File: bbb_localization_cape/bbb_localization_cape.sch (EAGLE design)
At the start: 32 parts, among them J2 MOLEX-22-03-5035, U1 SN65HVD256DR, U2 ARDUCAMOV5642, U3 SN74LV1T126DCKR, U4 MSP430G2553IPW20R, U5 SN74LV1T125DCKR, U6 LP38693MP-3.3/NOPB, U7 LM1085ISX-ADJ, U8 SN74LV1T126DCKR

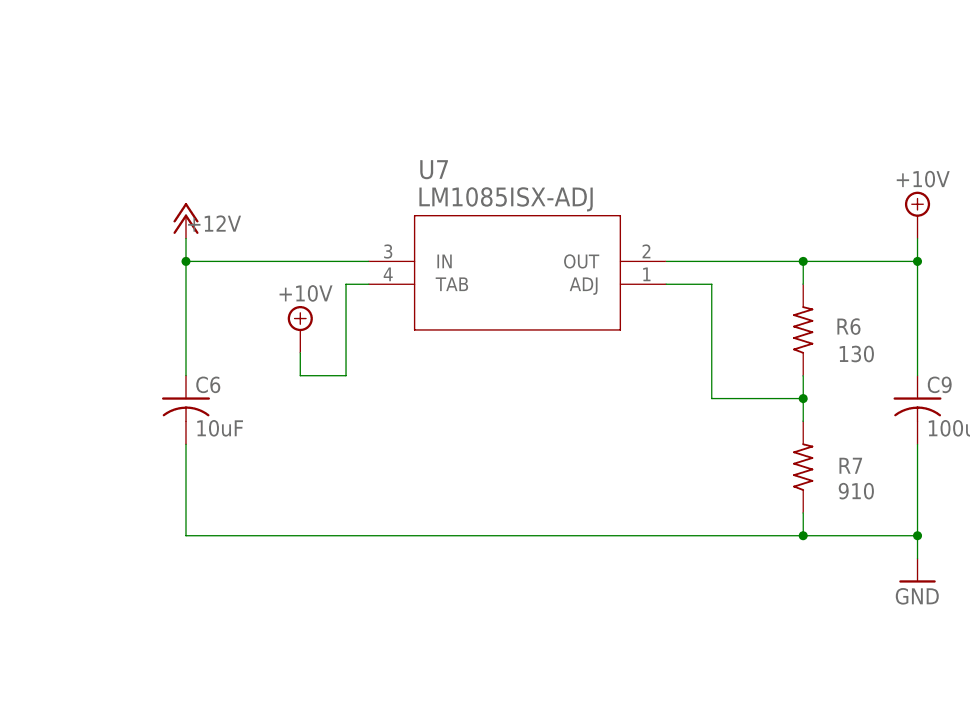
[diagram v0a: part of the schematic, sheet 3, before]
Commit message: Most of components placed
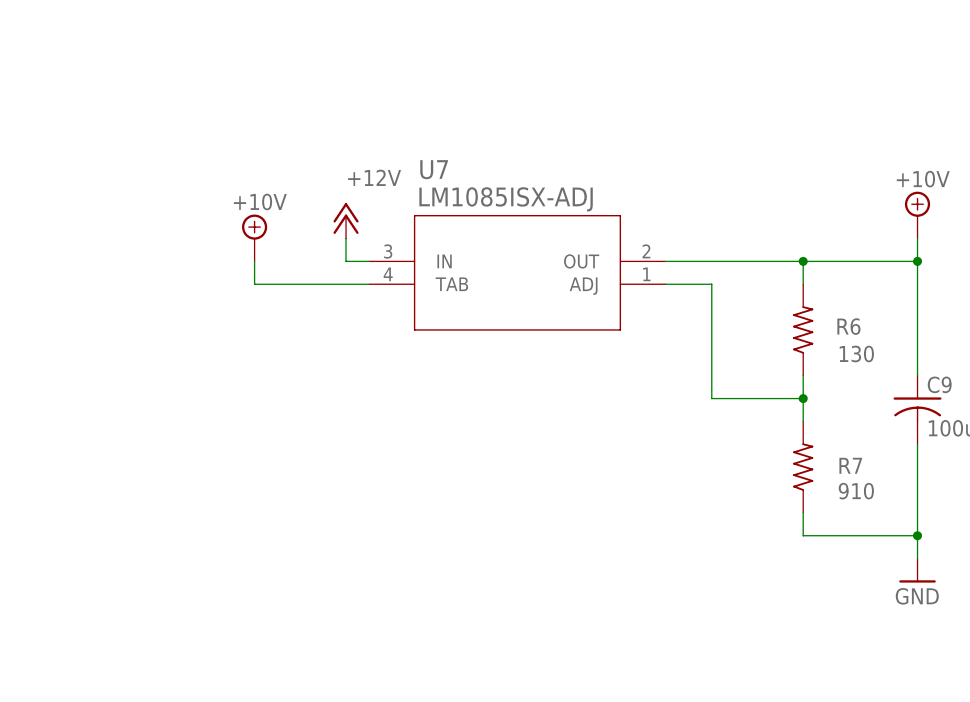
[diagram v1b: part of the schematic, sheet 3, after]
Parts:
- removed C6: 10uF, resistor:C-USC1206
- C2, C7, C8: device resistor:C-USC1206 -> resistor:C-USC0805
- R1, R2, R4, R5: device resistor:R-US_R1206 -> resistor:R-US_R0805
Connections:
- net +12V: no longer C6.1
- net GND: no longer C6.2
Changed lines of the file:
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@@
 <part name="P+10" library="supply1" library_urn="urn:adsk.eagle:library:371" deviceset="+5V" device=""/>
 <part name="GND11" library="supply1" library_urn="urn:adsk.eagle:library:371" deviceset="GND" device=""/>
-<part name="C8" library="resistor" library_urn="urn:adsk.eagle:library:348" deviceset="C-US" device="C1206" package3d_urn="urn:adsk.eagle:package:26140/1" value="4.7uF"/>
-<part name="C7" library="resistor" library_urn="urn:adsk.eagle:library:348" deviceset="C-US" device="C1206" package3d_urn="urn:adsk.eagle:package:26140/1" value="1uF"/>
+<part name="C8" library="resistor" library_urn="urn:adsk.eagle:library:348" deviceset="C-US" device="C0805" package3d_urn="urn:adsk.eagle:package:26137/1" value="4.7uF"/>
+<part name="C7" library="resistor" library_urn="urn:adsk.eagle:library:348" deviceset="C-US" device="C0805" package3d_urn="urn:adsk.eagle:package:26137/1" value="1uF"/>
 <part name="P+8" library="supply1" library_urn="urn:adsk.eagle:library:371" deviceset="+5V" device=""/>
 <part name="+3V38" library="supply1" library_urn="urn:adsk.eagle:library:371" deviceset="+3V3" device=""/>
@@
 <part name="C5" library="resistor" library_urn="urn:adsk.eagle:library:348" deviceset="C-US" device="C0805" package3d_urn="urn:adsk.eagle:package:26137/1" value="22uF"/>
 <part name="C9" library="resistor" library_urn="urn:adsk.eagle:library:348" deviceset="C-US" device="C1210" package3d_urn="urn:adsk.eagle:package:26139/1" value="100uF"/>
-<part name="C6" library="resistor" library_urn="urn:adsk.eagle:library:348" deviceset="C-US" device="C1206" package3d_urn="urn:adsk.eagle:package:26140/1" value="10uF"/>
 <part name="C3" library="resistor" library_urn="urn:adsk.eagle:library:348" deviceset="C-US" device="C0805" package3d_urn="urn:adsk.eagle:package:26137/1" value="10uF"/>
 <part name="U4" library="bbb_cape_parts" deviceset="MSP430G2553IPW20R" device=""/>
 <part name="+3V35" library="supply1" library_urn="urn:adsk.eagle:library:371" deviceset="+3V3" device=""/>
 <part name="+3V37" library="supply1" library_urn="urn:adsk.eagle:library:371" deviceset="+3V3" device=""/>
-<part name="R5" library="resistor" library_urn="urn:adsk.eagle:library:348" deviceset="R-US_" device="R1206" package3d_urn="urn:adsk.eagle:package:26062/1" value="47k"/>
-<part name="C2" library="resistor" library_urn="urn:adsk.eagle:library:348" deviceset="C-US" device="C1206" package3d_urn="urn:adsk.eagle:package:26140/1" value="100nF"/>
+<part name="R5" library="resistor" library_urn="urn:adsk.eagle:library:348" deviceset="R-US_" device="R0805" package3d_urn="urn:adsk.eagle:package:26059/1" value="47k"/>
+<part name="C2" library="resistor" library_urn="urn:adsk.eagle:library:348" deviceset="C-US" device="C0805" package3d_urn="urn:adsk.eagle:package:26137/1" value="100nF"/>
 <part name="GND8" library="supply1" library_urn="urn:adsk.eagle:library:371" deviceset="GND" device=""/>
 <part name="JP1" library="pinhead" library_urn="urn:adsk.eagle:library:325" deviceset="PINHD-1X4" device="" package3d_urn="urn:adsk.eagle:package:22407/2"/>
@@
 <part name="U2" library="bbb_localization_cape" deviceset="ARDUCAM" device="OV5642"/>
 <part name="+3V33" library="supply1" library_urn="urn:adsk.eagle:library:371" deviceset="+3V3" device=""/>
-<part name="R1" library="resistor" library_urn="urn:adsk.eagle:library:348" deviceset="R-US_" device="R1206" package3d_urn="urn:adsk.eagle:package:26062/1" value="10k"/>
-<part name="R2" library="resistor" library_urn="urn:adsk.eagle:library:348" deviceset="R-US_" device="R1206" package3d_urn="urn:adsk.eagle:package:26062/1" value="10k"/>
+<part name="R1" library="resistor" library_urn="urn:adsk.eagle:library:348" deviceset="R-US_" device="R0805" package3d_urn="urn:adsk.eagle:package:26059/1" value="10k"/>
+<part name="R2" library="resistor" library_urn="urn:adsk.eagle:library:348" deviceset="R-US_" device="R0805" package3d_urn="urn:adsk.eagle:package:26059/1" value="10k"/>
 <part name="+3V32" library="supply1" library_urn="urn:adsk.eagle:library:371" deviceset="+3V3" device=""/>
 <part name="+3V34" library="supply1" library_urn="urn:adsk.eagle:library:371" deviceset="+3V3" device=""/>
@@
 <part name="SJ1" library="jumper" library_urn="urn:adsk.eagle:library:252" deviceset="SJ2W" device="" package3d_urn="urn:adsk.eagle:package:15474/1"/>
 <part name="GND5" library="supply1" library_urn="urn:adsk.eagle:library:371" deviceset="GND" device=""/>
-<part name="R4" library="resistor" library_urn="urn:adsk.eagle:library:348" deviceset="R-US_" device="R1206" package3d_urn="urn:adsk.eagle:package:26062/1" value="10k"/>
+<part name="R4" library="resistor" library_urn="urn:adsk.eagle:library:348" deviceset="R-US_" device="R0805" package3d_urn="urn:adsk.eagle:package:26059/1" value="10k"/>
 <part name="J2" library="bbb_localization_cape" deviceset="MOLEX-22-03-5035" device=""/>
 <part name="GND6" library="supply1" library_urn="urn:adsk.eagle:library:371" deviceset="GND" device=""/>
@@
 <attribute name="VALUE" x="53.34" y="172.72" size="1.778" layer="96"/>
 </instance>
-<instance part="P+9" gate="1" x="144.78" y="104.14" smashed="yes">
-<attribute name="VALUE" x="144.78" y="104.14" size="1.778" layer="96" rot="MR180"/>
+<instance part="P+9" gate="1" x="162.56" y="104.14" smashed="yes">
+<attribute name="VALUE" x="162.56" y="109.22" size="1.778" layer="96" rot="MR180"/>
 </instance>
 <instance part="SUPPLY2" gate="G$1" x="226.06" y="104.14"/>
@@
 <instance part="C5" gate="G$1" x="96.52" y="66.04"/>
 <instance part="C9" gate="G$1" x="226.06" y="83.82"/>
-<instance part="C6" gate="G$1" x="144.78" y="83.82"/>
 <instance part="C3" gate="G$1" x="50.8" y="66.04"/>
 <instance part="GND10" gate="1" x="96.52" y="50.8"/>
 <instance part="FRAME3" gate="G$1" x="0" y="0"/>
 <instance part="FRAME3" gate="G$2" x="172.72" y="0"/>
-<instance part="SUPPLY3" gate="G$1" x="157.48" y="91.44"/>
+<instance part="SUPPLY3" gate="G$1" x="152.4" y="101.6"/>
 <instance part="U8" gate="A" x="111.76" y="160.02" smashed="yes">
 <attribute name="NAME" x="119.9896" y="169.1386" size="2.0828" layer="95" ratio="6" rot="SR0"/>
@@
 <wire x1="226.06" y1="78.74" x2="226.06" y2="68.58" width="0.1524" layer="91"/>
 <junction x="226.06" y="68.58"/>
-<pinref part="C6" gate="G$1" pin="2"/>
-<wire x1="144.78" y1="78.74" x2="144.78" y2="68.58" width="0.1524" layer="91"/>
-<wire x1="144.78" y1="68.58" x2="213.36" y2="68.58" width="0.1524" layer="91"/>
-<junction x="213.36" y="68.58"/>
 </segment>
 <segment>
@@
 <segment>
 <pinref part="P+9" gate="1" pin="+12V"/>
-<wire x1="144.78" y1="101.6" x2="144.78" y2="99.06" width="0.1524" layer="91"/>
+<wire x1="162.56" y1="101.6" x2="162.56" y2="99.06" width="0.1524" layer="91"/>
 <pinref part="U7" gate="A" pin="IN"/>
-<wire x1="165.1" y1="99.06" x2="144.78" y2="99.06" width="0.1524" layer="91"/>
-<pinref part="C6" gate="G$1" pin="1"/>
-<wire x1="144.78" y1="86.36" x2="144.78" y2="99.06" width="0.1524" layer="91"/>
-<junction x="144.78" y="99.06"/>
+<wire x1="165.1" y1="99.06" x2="162.56" y2="99.06" width="0.1524" layer="91"/>
 </segment>
 <segment>
@@
 <segment>
 <pinref part="SUPPLY3" gate="G$1" pin="+10V"/>
-<wire x1="157.48" y1="88.9" x2="157.48" y2="86.36" width="0.1524" layer="91"/>
-<wire x1="157.48" y1="86.36" x2="162.56" y2="86.36" width="0.1524" layer="91"/>
+<wire x1="152.4" y1="99.06" x2="152.4" y2="96.52" width="0.1524" layer="91"/>
 <pinref part="U7" gate="A" pin="TAB"/>
-<wire x1="165.1" y1="96.52" x2="162.56" y2="96.52" width="0.1524" layer="91"/>
-<wire x1="162.56" y1="86.36" x2="162.56" y2="96.52" width="0.1524" layer="91"/>
-</segment>
-</net>
+<wire x1="152.4" y1="96.52" x2="165.1" y2="96.52" width="0.1524" layer="91"/>
+</segment>
+</net>

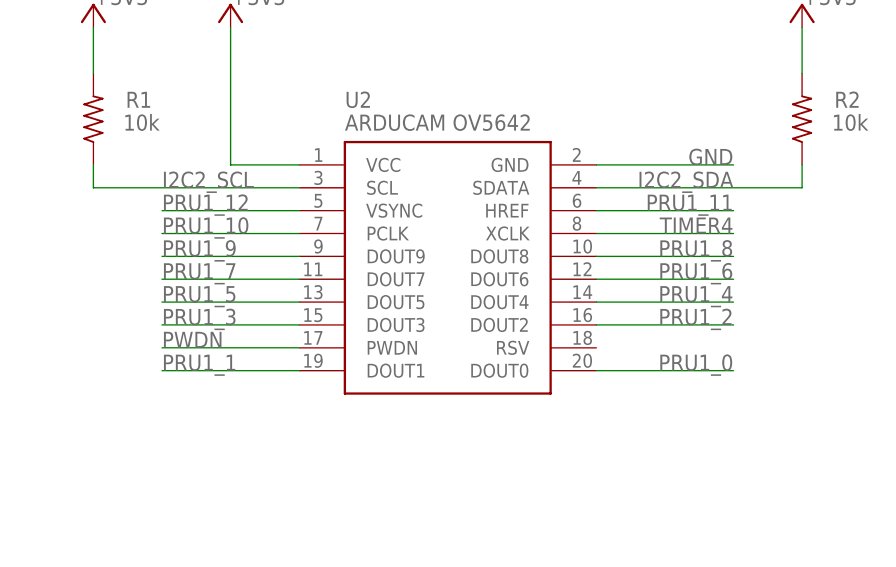
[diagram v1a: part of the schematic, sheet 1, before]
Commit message: Laid out most of camera module traces
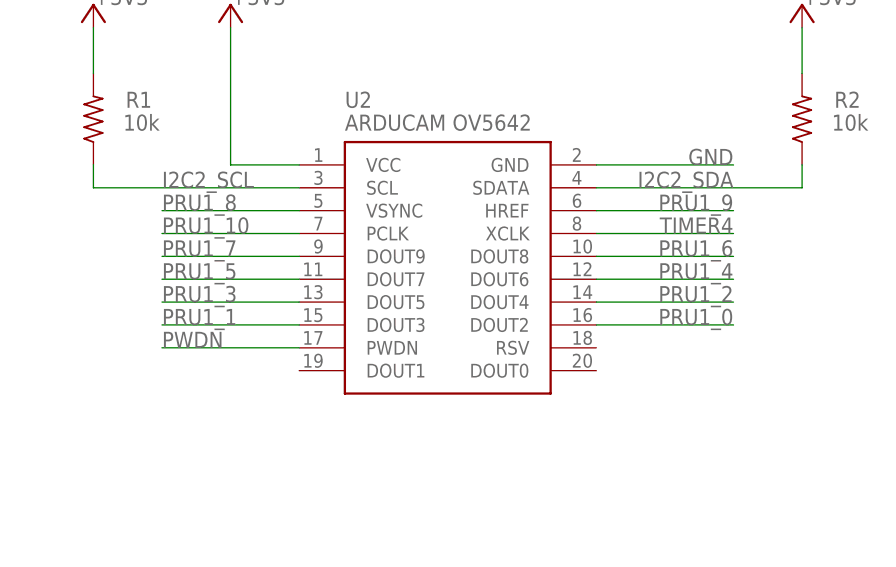
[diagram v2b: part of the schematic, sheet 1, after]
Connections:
- net PRU1_0: now also U2.DOUT2; no longer U2.DOUT0
- net PRU1_1: now also U2.DOUT3; no longer U2.DOUT1
- net PRU1_11: no longer U2.HREF
- net PRU1_12: no longer U2.VSYNC
- net PRU1_2: now also U2.DOUT4; no longer U2.DOUT2
- net PRU1_3: now also U2.DOUT5; no longer U2.DOUT3
- net PRU1_4: now also U2.DOUT6; no longer U2.DOUT4
- net PRU1_5: now also U2.DOUT7; no longer U2.DOUT5
- net PRU1_6: now also U2.DOUT8; no longer U2.DOUT6
- net PRU1_7: now also U2.DOUT9; no longer U2.DOUT7
- net PRU1_8: now also U2.VSYNC; no longer U2.DOUT8
- net PRU1_9: now also U2.HREF; no longer U2.DOUT9
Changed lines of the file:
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@@
 <class number="0" name="default" width="0" drill="0">
+</class>
+<class number="1" name="PRU" width="0.254" drill="0.254">
+<clearance class="1" value="0.254"/>
 </class>
 </classes>
@@
 </segment>
 </net>
-<net name="PRU1_1" class="0">
+<net name="PRU1_1" class="1">
 <segment>
 <pinref part="A1" gate="G$1" pin="46@P8"/>
@@
 </segment>
 <segment>
-<pinref part="U2" gate="&gt;NAME" pin="DOUT1"/>
-<wire x1="198.12" y1="45.72" x2="182.88" y2="45.72" width="0.1524" layer="91"/>
-<label x="182.88" y="45.72" size="1.778" layer="95"/>
-</segment>
-</net>
-<net name="PRU1_3" class="0">
+<pinref part="U2" gate="&gt;NAME" pin="DOUT3"/>
+<wire x1="198.12" y1="50.8" x2="182.88" y2="50.8" width="0.1524" layer="91"/>
+<label x="182.88" y="50.8" size="1.778" layer="95"/>
+</segment>
+</net>
+<net name="PRU1_3" class="1">
 <segment>
 <pinref part="A1" gate="G$1" pin="44@P8"/>
@@
 </segment>
 <segment>
-<pinref part="U2" gate="&gt;NAME" pin="DOUT3"/>
-<wire x1="198.12" y1="50.8" x2="182.88" y2="50.8" width="0.1524" layer="91"/>
-<label x="182.88" y="50.8" size="1.778" layer="95"/>
-</segment>
-</net>
-<net name="PRU1_5" class="0">
+<pinref part="U2" gate="&gt;NAME" pin="DOUT5"/>
+<wire x1="198.12" y1="53.34" x2="182.88" y2="53.34" width="0.1524" layer="91"/>
+<label x="182.88" y="53.34" size="1.778" layer="95"/>
+</segment>
+</net>
+<net name="PRU1_5" class="1">
 <segment>
 <pinref part="A1" gate="G$1" pin="42@P8"/>
@@
 </segment>
 <segment>
-<pinref part="U2" gate="&gt;NAME" pin="DOUT5"/>
-<wire x1="198.12" y1="53.34" x2="182.88" y2="53.34" width="0.1524" layer="91"/>
-<label x="182.88" y="53.34" size="1.778" layer="95"/>
-</segment>
-</net>
-<net name="PRU1_7" class="0">
+<pinref part="U2" gate="&gt;NAME" pin="DOUT7"/>
+<wire x1="198.12" y1="55.88" x2="182.88" y2="55.88" width="0.1524" layer="91"/>
+<label x="182.88" y="55.88" size="1.778" layer="95"/>
+</segment>
+</net>
+<net name="PRU1_7" class="1">
 <segment>
 <pinref part="A1" gate="G$1" pin="40@P8"/>
@@
 </segment>
 <segment>
-<pinref part="U2" gate="&gt;NAME" pin="DOUT7"/>
-<wire x1="198.12" y1="55.88" x2="182.88" y2="55.88" width="0.1524" layer="91"/>
-<label x="182.88" y="55.88" size="1.778" layer="95"/>
-</segment>
-</net>
-<net name="PRU1_0" class="0">
+<pinref part="U2" gate="&gt;NAME" pin="DOUT9"/>
+<wire x1="198.12" y1="58.42" x2="182.88" y2="58.42" width="0.1524" layer="91"/>
+<label x="182.88" y="58.42" size="1.778" layer="95"/>
+</segment>
+</net>
+<net name="PRU1_0" class="1">
 <segment>
 <pinref part="A1" gate="G$1" pin="45@P8"/>
@@
 </segment>
 <segment>
-<pinref part="U2" gate="&gt;NAME" pin="DOUT0"/>
-<wire x1="231.14" y1="45.72" x2="246.38" y2="45.72" width="0.1524" layer="91"/>
-<label x="246.38" y="45.72" size="1.778" layer="95" rot="MR0"/>
-</segment>
-</net>
-<net name="PRU1_2" class="0">
+<pinref part="U2" gate="&gt;NAME" pin="DOUT2"/>
+<wire x1="231.14" y1="50.8" x2="246.38" y2="50.8" width="0.1524" layer="91"/>
+<label x="246.38" y="50.8" size="1.778" layer="95" rot="MR0"/>
+</segment>
+</net>
+<net name="PRU1_2" class="1">
 <segment>
 <pinref part="A1" gate="G$1" pin="43@P8"/>
@@
 </segment>
 <segment>
-<pinref part="U2" gate="&gt;NAME" pin="DOUT2"/>
-<wire x1="231.14" y1="50.8" x2="246.38" y2="50.8" width="0.1524" layer="91"/>
-<label x="246.38" y="50.8" size="1.778" layer="95" rot="MR0"/>
-</segment>
-</net>
-<net name="PRU1_4" class="0">
+<pinref part="U2" gate="&gt;NAME" pin="DOUT4"/>
+<wire x1="231.14" y1="53.34" x2="246.38" y2="53.34" width="0.1524" layer="91"/>
+<label x="246.38" y="53.34" size="1.778" layer="95" rot="MR0"/>
+</segment>
+</net>
+<net name="PRU1_4" class="1">
 <segment>
 <pinref part="A1" gate="G$1" pin="41@P8"/>
@@
 </segment>
 <segment>
-<pinref part="U2" gate="&gt;NAME" pin="DOUT4"/>
-<wire x1="231.14" y1="53.34" x2="246.38" y2="53.34" width="0.1524" layer="91"/>
-<label x="246.38" y="53.34" size="1.778" layer="95" rot="MR0"/>
-</segment>
-</net>
-<net name="PRU1_6" class="0">
+<pinref part="U2" gate="&gt;NAME" pin="DOUT6"/>
+<wire x1="231.14" y1="55.88" x2="246.38" y2="55.88" width="0.1524" layer="91"/>
+<label x="246.38" y="55.88" size="1.778" layer="95" rot="MR0"/>
+</segment>
+</net>
+<net name="PRU1_6" class="1">
 <segment>
 <pinref part="A1" gate="G$1" pin="39@P8"/>
@@
 </segment>
 <segment>
-<pinref part="U2" gate="&gt;NAME" pin="DOUT6"/>
-<wire x1="231.14" y1="55.88" x2="246.38" y2="55.88" width="0.1524" layer="91"/>
-<label x="246.38" y="55.88" size="1.778" layer="95" rot="MR0"/>
-</segment>
-</net>
-<net name="PRU1_9" class="0">
+<pinref part="U2" gate="&gt;NAME" pin="DOUT8"/>
+<wire x1="231.14" y1="58.42" x2="246.38" y2="58.42" width="0.1524" layer="91"/>
+<label x="246.38" y="58.42" size="1.778" layer="95" rot="MR0"/>
+</segment>
+</net>
+<net name="PRU1_9" class="1">
 <segment>
 <pinref part="A1" gate="G$1" pin="29@P8"/>
@@
 </segment>
 <segment>
-<pinref part="U2" gate="&gt;NAME" pin="DOUT9"/>
-<wire x1="198.12" y1="58.42" x2="182.88" y2="58.42" width="0.1524" layer="91"/>
-<label x="182.88" y="58.42" size="1.778" layer="95"/>
-</segment>
-</net>
-<net name="PRU1_8" class="0">
+<pinref part="U2" gate="&gt;NAME" pin="HREF"/>
+<wire x1="231.14" y1="63.5" x2="246.38" y2="63.5" width="0.1524" layer="91"/>
+<label x="246.38" y="63.5" size="1.778" layer="95" rot="MR0"/>
+</segment>
+</net>
+<net name="PRU1_8" class="1">
 <segment>
 <pinref part="A1" gate="G$1" pin="27@P8"/>
@@
 </segment>
 <segment>
-<pinref part="U2" gate="&gt;NAME" pin="DOUT8"/>
-<wire x1="231.14" y1="58.42" x2="246.38" y2="58.42" width="0.1524" layer="91"/>
-<label x="246.38" y="58.42" size="1.778" layer="95" rot="MR0"/>
-</segment>
-</net>
-<net name="PRU1_11" class="0">
+<pinref part="U2" gate="&gt;NAME" pin="VSYNC"/>
+<wire x1="198.12" y1="63.5" x2="182.88" y2="63.5" width="0.1524" layer="91"/>
+<label x="182.88" y="63.5" size="1.778" layer="95"/>
+</segment>
+</net>
+<net name="PRU1_11" class="1">
 <segment>
 <pinref part="A1" gate="G$1" pin="30@P8"/>
@@
 <label x="129.54" y="152.4" size="1.778" layer="95" rot="MR0"/>
 </segment>
-<segment>
-<pinref part="U2" gate="&gt;NAME" pin="HREF"/>
-<wire x1="231.14" y1="63.5" x2="246.38" y2="63.5" width="0.1524" layer="91"/>
-<label x="246.38" y="63.5" size="1.778" layer="95" rot="MR0"/>
-</segment>
-</net>
-<net name="PRU1_10" class="0">
+</net>
+<net name="PRU1_10" class="1">
 <segment>
 <pinref part="A1" gate="G$1" pin="28@P8"/>
@@
 </segment>
 </net>
-<net name="TIMER4" class="0">
+<net name="TIMER4" class="1">
 <segment>
 <pinref part="A1" gate="G$1" pin="07@P8"/>
@@
 </segment>
 </net>
-<net name="PRU1_12" class="0">
-<segment>
-<pinref part="U2" gate="&gt;NAME" pin="VSYNC"/>
-<wire x1="198.12" y1="63.5" x2="182.88" y2="63.5" width="0.1524" layer="91"/>
-<label x="182.88" y="63.5" size="1.778" layer="95"/>
-</segment>
+<net name="PRU1_12" class="1">
 <segment>
 <pinref part="A1" gate="G$1" pin="21@P8"/>
@@
 </segment>
 </net>
-<net name="I2C2_SCL" class="0">
+<net name="I2C2_SCL" class="1">
 <segment>
 <pinref part="A1" gate="G$1" pin="19@P9"/>
@@
 </segment>
 </net>
-<net name="I2C2_SCL" class="0">
+<net name="I2C2_SCL" class="1">
 <segment>
 <pinref part="U4" gate="A" pin="P1.6/TA0.1/UCB0SOMI/UCB0SCL/A6/CA6/TDI/TCLK"/>
